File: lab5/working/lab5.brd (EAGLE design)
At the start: 40 x 40 mm, 52 parts, among them J1 ISP, Q1 FET, Q2 FET, Q3 FET, Q4 FET, U1 ATMEGA128RFA1, Y1 16MHz

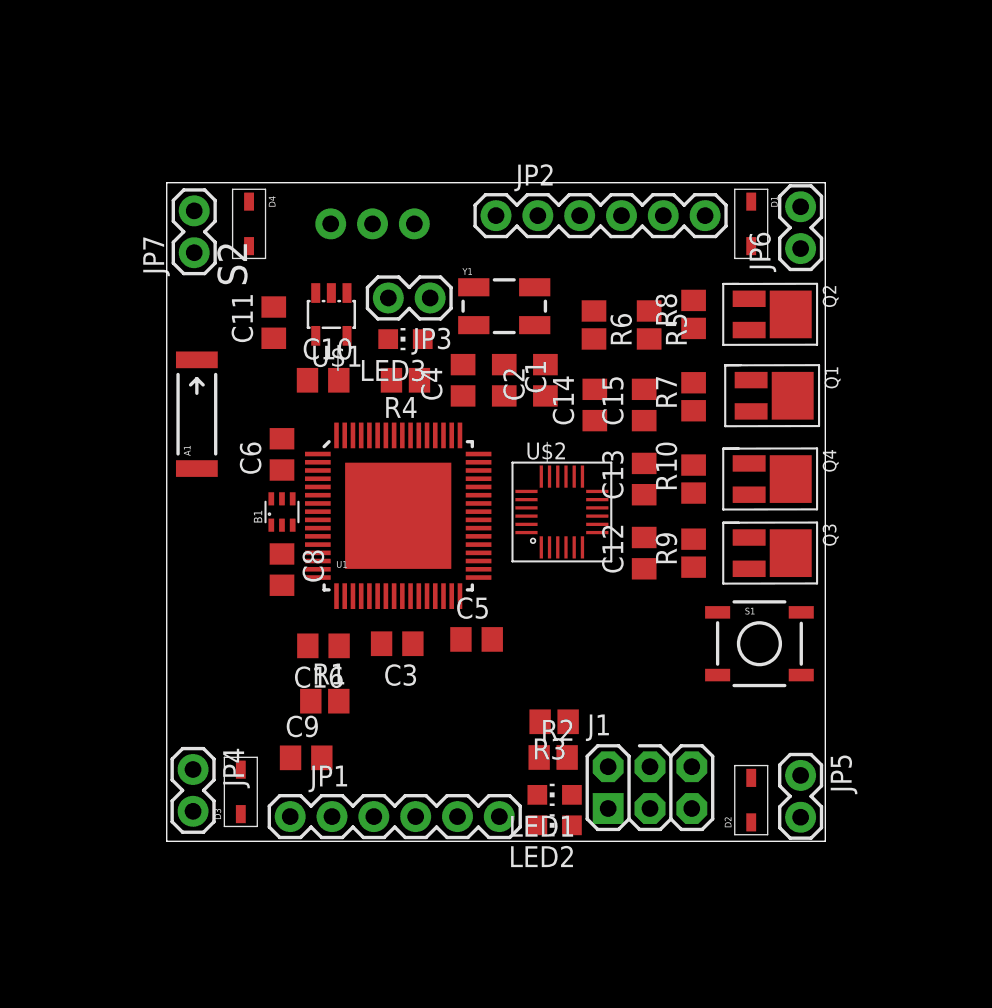
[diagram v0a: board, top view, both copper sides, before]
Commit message: made board circular
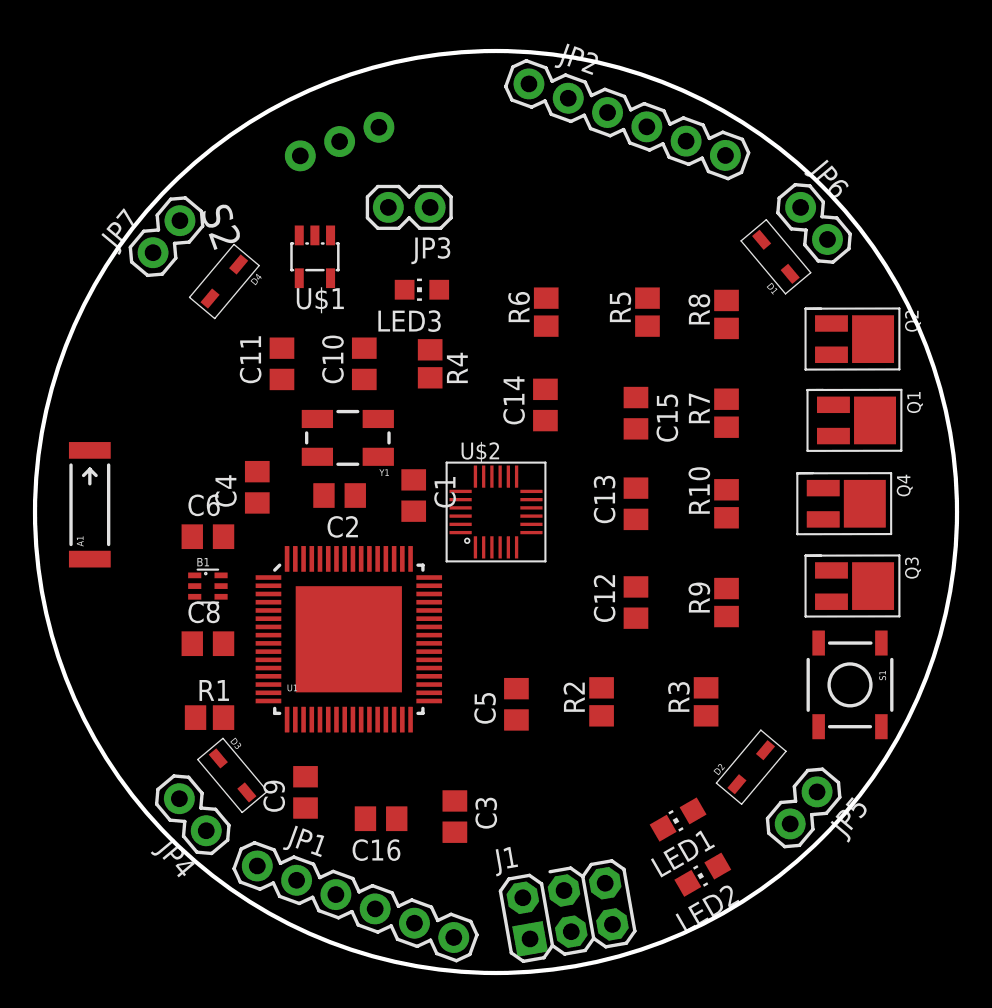
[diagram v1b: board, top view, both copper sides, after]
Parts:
- moved C2 14.3 mm to (-9.50, 1.00), turned to 180 degrees
- moved C4 14.1 mm to (-14.5, 1.50)
- moved Y1 12.4 mm to (-9.00, 4.50), turned to 180 degrees
- moved C3 11.1 mm to (-2.50, -18.5), turned to 270 degrees
- moved C16 11.1 mm to (-6.98, -18.6)
- moved LED2 9.49 mm to (12.6, -22.0), turned to 120 degrees
- moved R3 9.31 mm to (12.8, -11.5), turned to 90 degrees
- moved J1 9.01 mm to (4.35, -24.2), turned to 10 degrees
- moved C1 8.90 mm to (-5.00, 1.00)
- moved A1 8.51 mm to (-24.7, 0.44)
- moved JP2 8.25 mm to (2.00, 26.0), turned to 340 degrees
- moved U1 8.08 mm to (-8.94, -7.73)
- moved LED1 7.65 mm to (11.1, -18.7), turned to 120 degrees
- moved R1 7.07 mm to (-17.4, -12.5)
- moved C6 6.73 mm to (-17.5, -1.50), turned to 0 degrees
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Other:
- board size 40 x 40 mm -> 56 x 56 mm

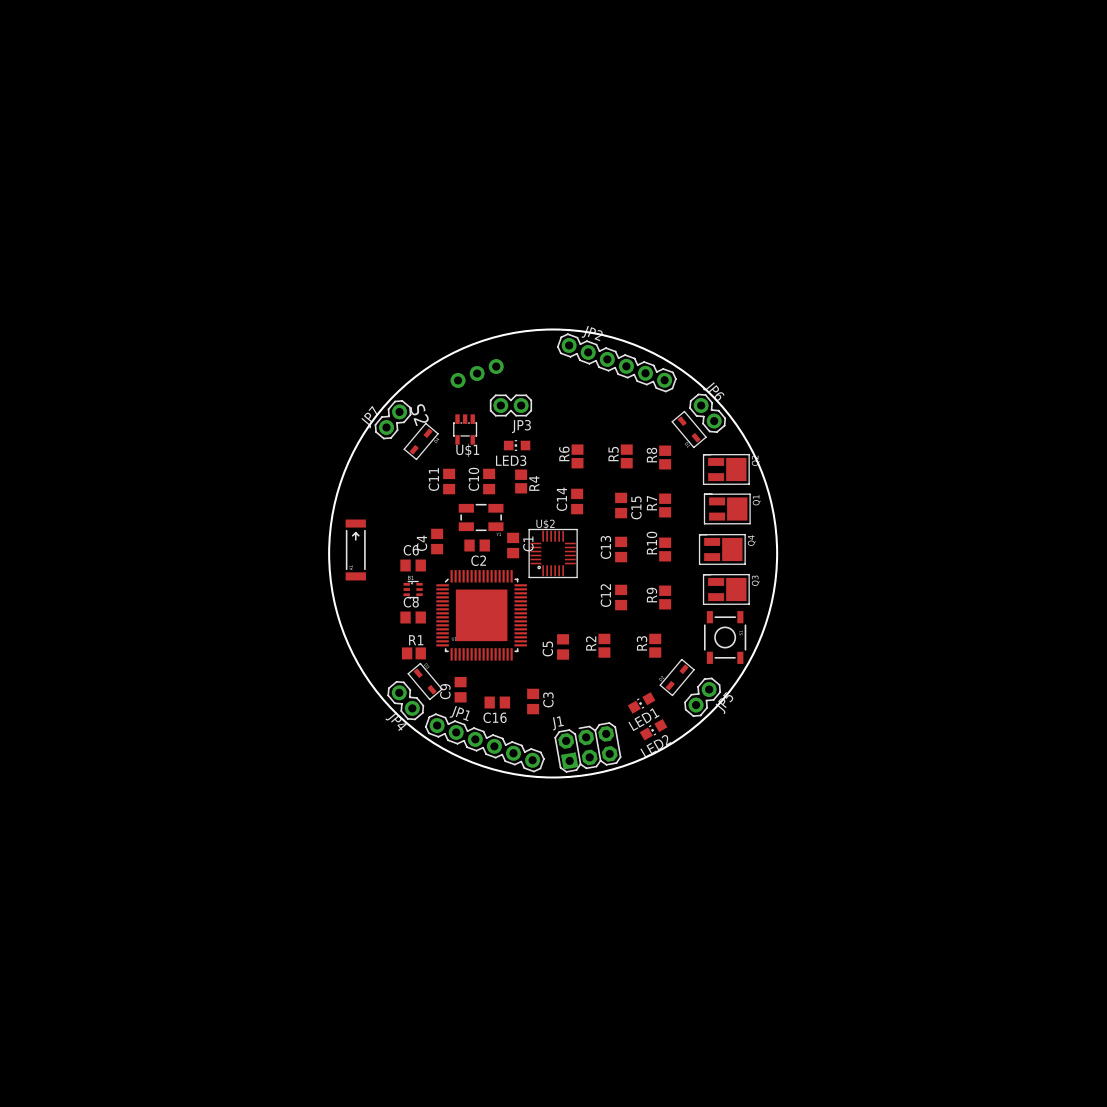
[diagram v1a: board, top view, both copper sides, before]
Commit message: added motor arms but still need to be aligned precisely
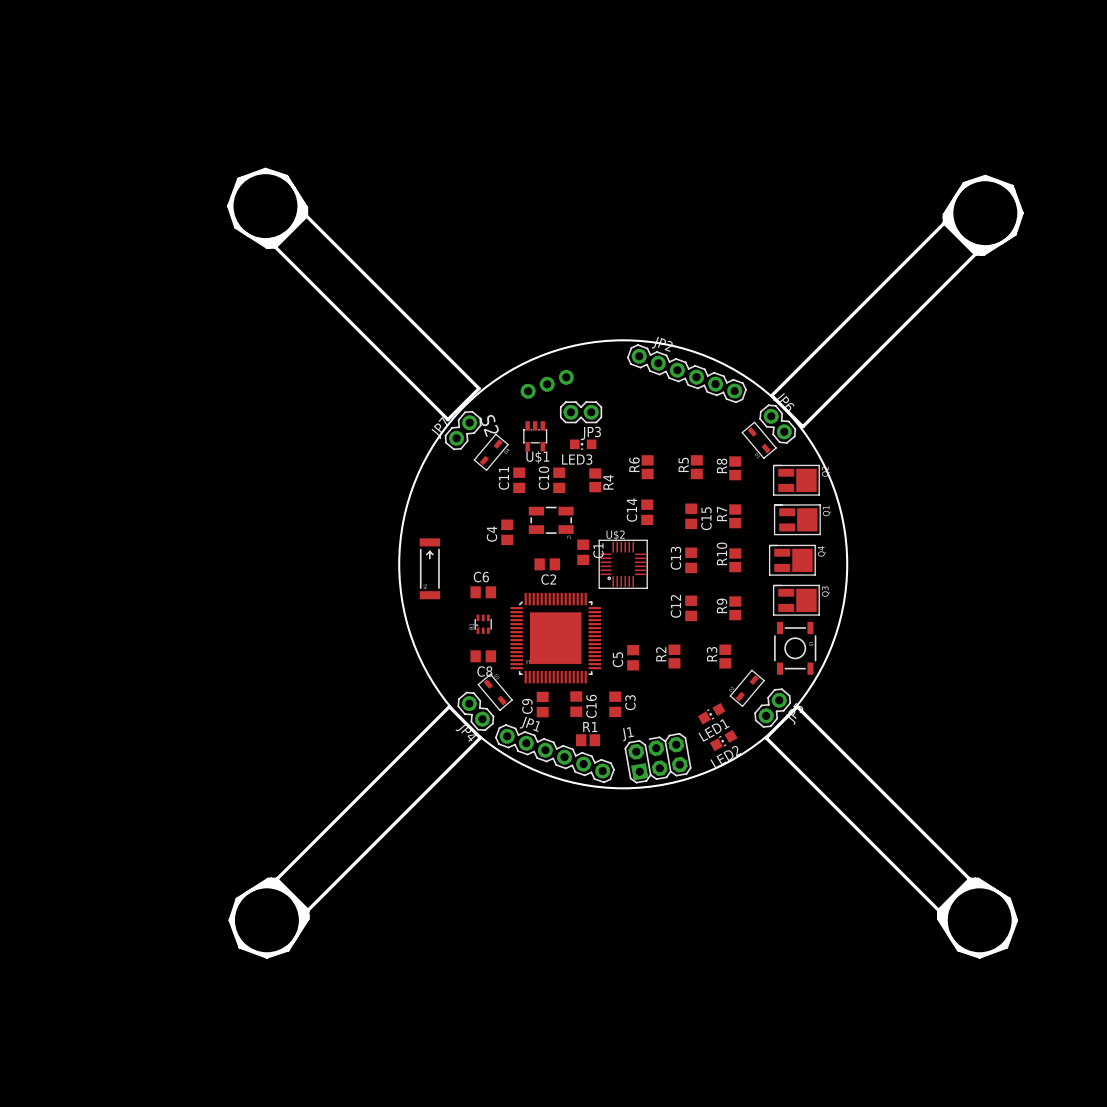
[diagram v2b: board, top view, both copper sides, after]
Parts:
- moved R1 24.3 mm to (4.36, -23.3)
- moved C9 10.4 mm to (-1.31, -18.9)
- moved C3 10.3 mm to (7.76, -18.9)
- moved C8 10.0 mm to (-8.74, -12.9), turned to 180 degrees
- moved C16 9.87 mm to (2.89, -18.8), turned to 270 degrees
- moved B1 9.78 mm to (-8.74, -8.85), turned to 0 degrees
- moved U1 9.69 mm to (0.32, -10.6)
- moved A1 9.55 mm to (-15.4, -1.91)
- moved C6 9.38 mm to (-8.74, -4.85)
- moved R4 9.26 mm to (5.26, 9.15)
- moved C2 9.07 mm to (-0.74, -1.35)
- moved JP7 8.86 mm to (-12.1, 14.4)
- moved JP1 8.86 mm to (-5.74, -22.9)
- moved S2 8.86 mm to (-0.74, 21.1)
- moved D4 8.86 mm to (-7.74, 12.6)
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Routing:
- net PE4: track 0.00 -> 17.9 mm
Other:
- board size 56 x 56 mm -> 99.2 x 98.5 mm

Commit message: Added ground planes and rotated
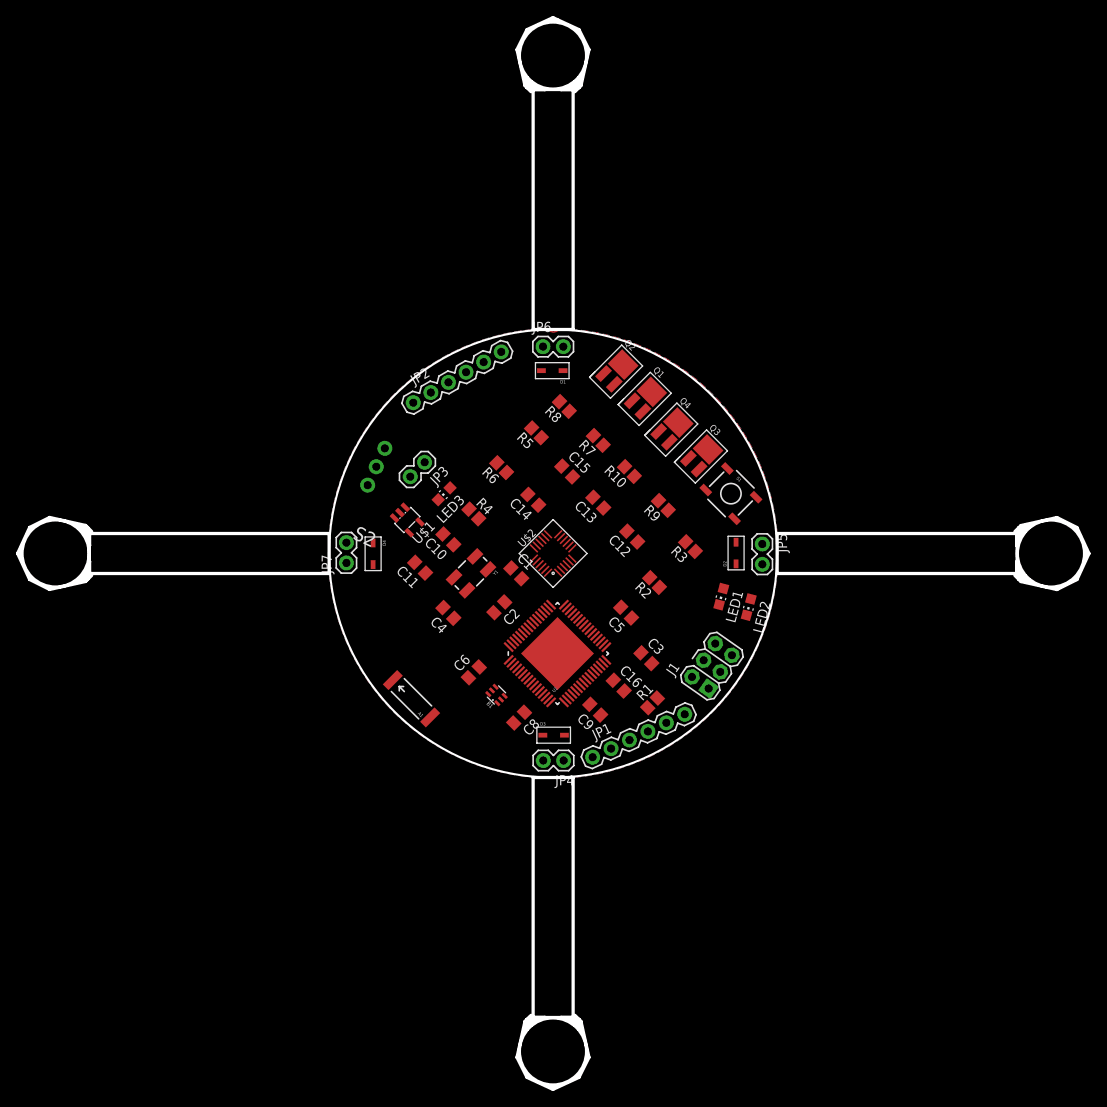
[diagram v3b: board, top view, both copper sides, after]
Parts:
- moved JP6 29.8 mm to (-1.26, 25.9), turned to 0 degrees
- moved JP2 28.8 mm to (-17.5, 18.9), turned to 30 degrees
- moved D1 27.3 mm to (-0.11, 22.9), turned to 180 degrees
- moved Q2 26.2 mm to (7.77, 22.6), turned to 315 degrees
- moved Q1 24.2 mm to (11.3, 19.2), turned to 315 degrees
- moved S2 23.7 mm to (-22.1, 10.8), turned to 155 degrees
- moved R8 22.7 mm to (1.40, 18.4), turned to 135 degrees
- moved Q4 22.2 mm to (14.7, 15.4), turned to 315 degrees
- moved JP3 21.7 mm to (-16.1, 11.4), turned to 225 degrees
- moved Q3 21.5 mm to (18.4, 12.0), turned to 315 degrees
- moved S1 20.9 mm to (22.2, 7.48), turned to 315 degrees
- moved JP7 20.8 mm to (-25.8, -1.18), turned to 90 degrees
- moved R5 20.5 mm to (-2.09, 15.1), turned to 135 degrees
- moved JP5 19.6 mm to (26.1, 1.19), turned to 270 degrees
- moved R7 19.6 mm to (5.65, 14.1), turned to 135 degrees
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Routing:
- added copper zone on layer 1, net GND
- added copper zone on layer 16, net GND
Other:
- board size 99.2 x 98.5 mm -> 133.9 x 134 mm

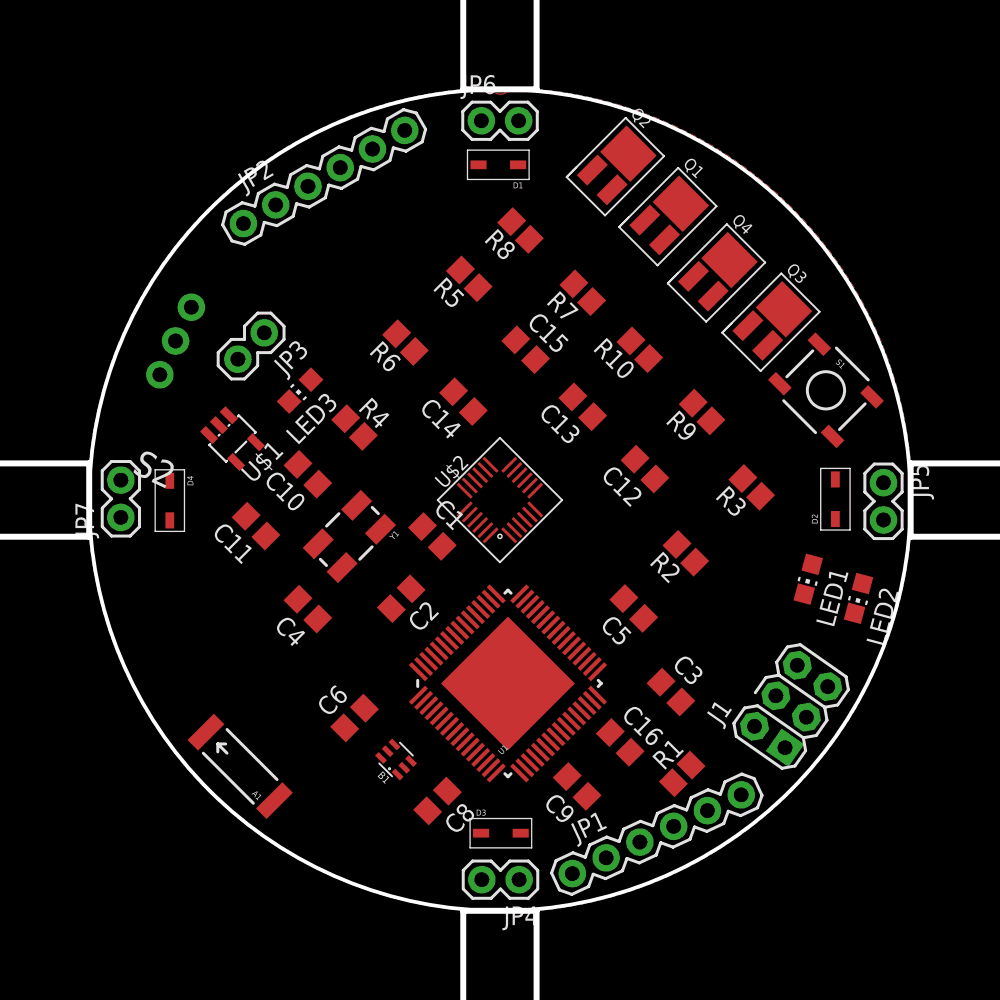
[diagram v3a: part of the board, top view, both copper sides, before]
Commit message: added radio circuit
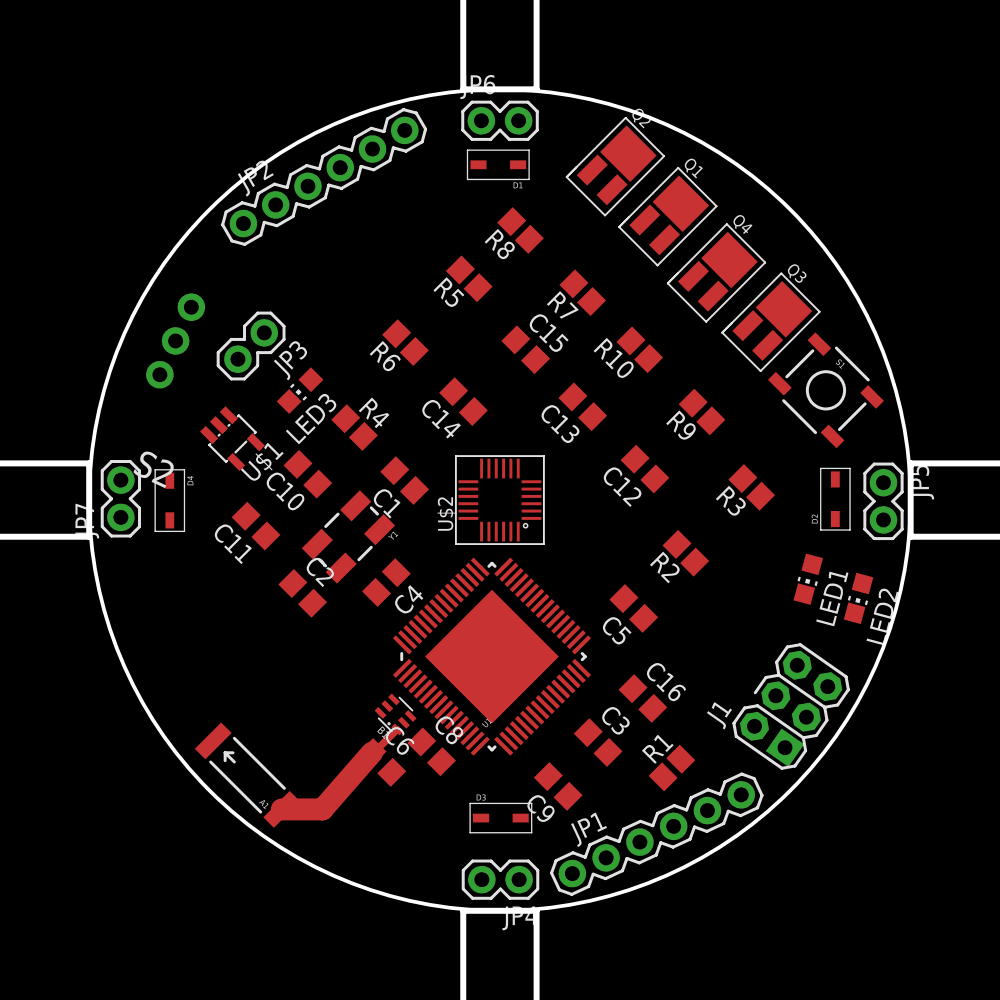
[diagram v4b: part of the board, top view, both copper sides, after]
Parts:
- moved C2 6.73 mm to (-13.4, -6.36), turned to 315 degrees
- moved C3 6.04 mm to (6.70, -16.5)
- moved C4 5.65 mm to (-7.74, -5.62), turned to 225 degrees
- moved C1 4.25 mm to (-6.49, 1.33), turned to 135 degrees
- moved C6 3.56 mm to (-8.05, -17.9), turned to 315 degrees
- moved C8 3.37 mm to (-4.66, -17.2), turned to 315 degrees
- moved C16 3.37 mm to (9.75, -13.5)
- moved B1 3.07 mm to (-7.11, -14.6)
- moved U1 2.13 mm to (-0.54, -10.7)
- moved C9 1.29 mm to (3.97, -19.5)
- moved D3 1.03 mm to (0.07, -21.7)
- moved R1 0.81 mm to (11.7, -18.3)
- moved A1 0.78 mm to (-17.2, -18.8)
- moved Y1 0.07 mm to (-10.3, -2.51)
- turned U$2 to 90 degrees
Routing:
- net PE4: track 17.9 -> 0.00 mm
- net N$4: track 0.00 -> 10.3 mm
- removed copper zone on layer 1, net GND
- removed copper zone on layer 16, net GND

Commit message: fixed radio
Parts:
- moved B1 0.97 mm to (-7.95, -14.1)
- moved C8 0.94 mm to (-5.33, -16.5)
- moved C6 0.90 mm to (-8.29, -17.0)
- moved D1 0.43 mm to (0.04, 22.5)
- moved JP5 0.40 mm to (25.7, 1.19)
- moved D2 0.39 mm to (22.5, 0.06)
- moved JP6 0.30 mm to (-1.26, 25.6)
- moved A1 0.19 mm to (-17.3, -18.9)
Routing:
- net N$4: track 10.3 -> 9.71 mm
- added copper zone on layer 1, net GND
- added copper zone on layer 16, net GND
